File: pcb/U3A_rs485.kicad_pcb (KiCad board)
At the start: 2 copper layers, 34.5 x 26.4 mm, 17 parts, among them J1 Screw_Terminal_01x06, J2 Conn_01x07_Socket, J3 Conn_01x02_Pin, J4 Conn_01x08_Socket, J5 Conn_01x02_Pin, U1 THVD1452DR

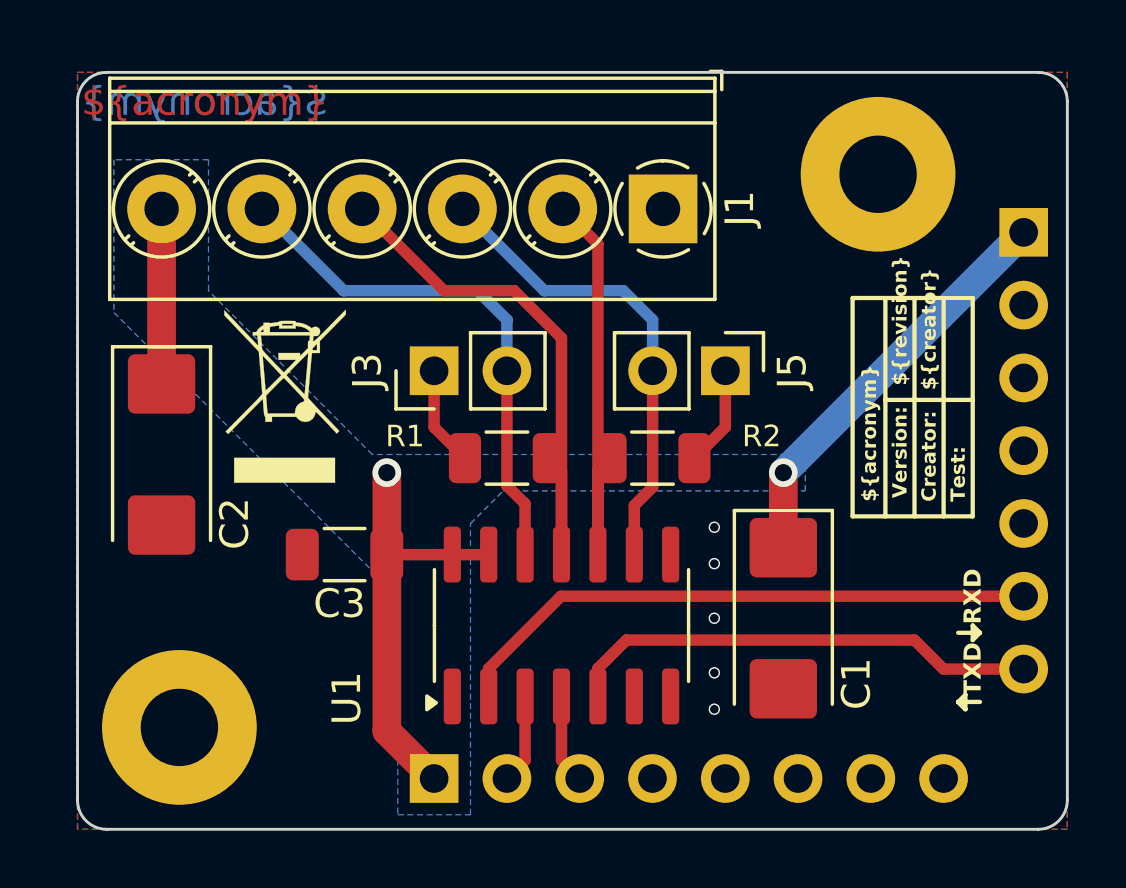
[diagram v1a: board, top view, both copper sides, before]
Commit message: Add missing pull-up resistor
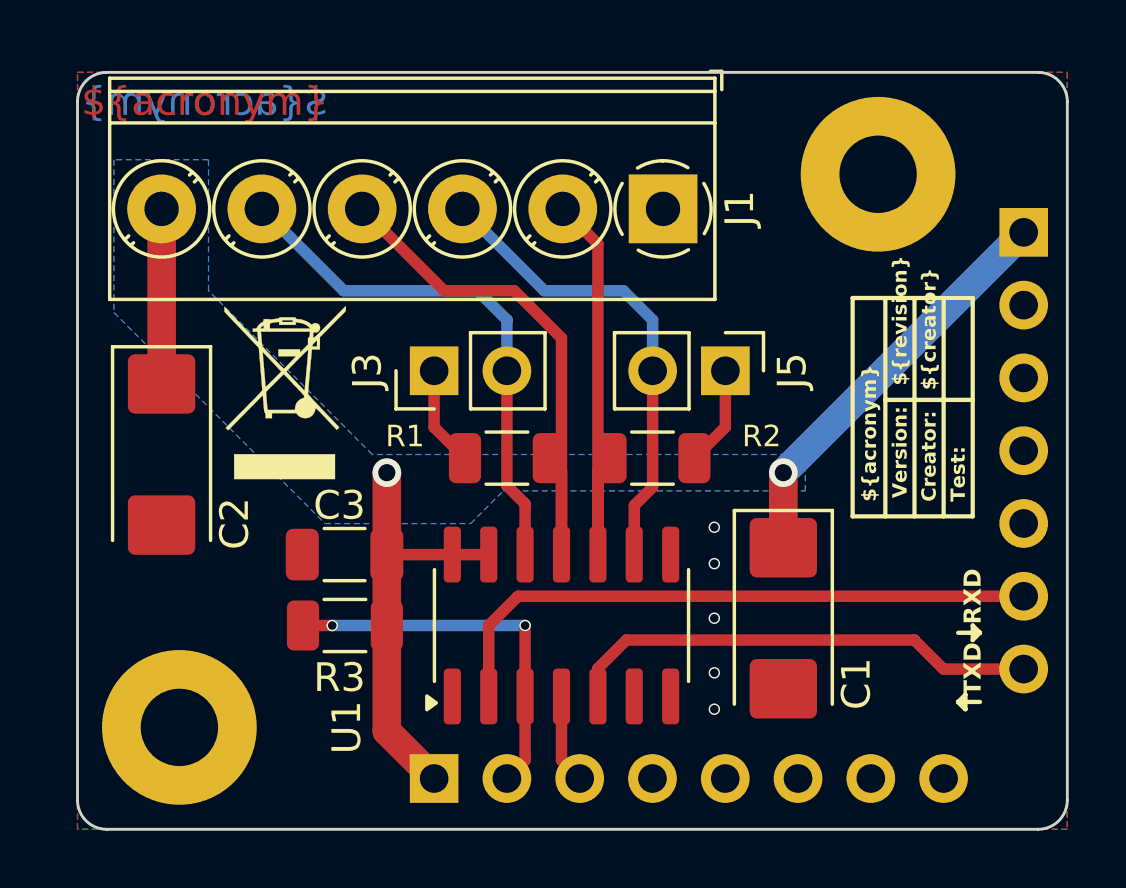
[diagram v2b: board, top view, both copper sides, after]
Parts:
- added R3: 10k, Resistor_SMD:R_1206_3216Metric, F.Cu at (154.1, 95.5)
- moved FID3 0.13 mm to (152.0, 87.4)
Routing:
- net /CBUS3: track 3.13 -> 13.4 mm, vias 0 -> 2
- net /RXD: track 20.7 -> 21.6 mm
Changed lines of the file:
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@@
   (net 20 "unconnected-(U1-NC-Pad1)")
   (net 21 "unconnected-(U1-NC-Pad8)")
+  (footprint "Resistor_SMD:R_1206_3216Metric" (layer "F.Cu")
+    (at 154.1125 95.504 180)
+    (descr "Resistor SMD 1206 (3216 Metric), square (rectangular) end terminal, IPC_7351 nominal, (Body size source: IPC-SM-782 page 72, https://www.pcb-3d.com/wordpress/wp-content/uploads/ipc-sm-782a_amendment_1_and_2.pdf), generated with kicad-footprint-generator")
+    (tags "resistor")
+    (property "Sheetfile" "U3A_rs485.kicad_sch")
+    (property "Sheetname" "")
+    (property "Vendor" "HTL")
+    (property "VendorId" "102967")
+    (property "ki_description" "Resistor")
+    (property "ki_keywords" "R res resistor")
+    (attr smd)
+    (fp_text reference "R3" (at 0.1885 -1.82) (layer "F.SilkS")
+        (effects (font (size 1 1) (thickness 0.15)))
+    )
+    (fp_text value "10k" (at 0 -1.778) (layer "F.Fab")
+        (effects (font (size 1 1) (thickness 0.15)))
+    )
+    (fp_text user "${REFERENCE}" (at 0 0) (layer "F.Fab")
+        (effects (font (size 0.8 0.8) (thickness 0.12)))
+    )
+    (fp_line (start -0.727064 -0.91) (end 0.727064 -0.91)
+      (stroke (width 0.12) (type solid)) (layer "F.SilkS"))
+    (fp_line (start -0.727064 0.91) (end 0.727064 0.91)
+      (stroke (width 0.12) (type solid)) (layer "F.SilkS"))
+    (fp_line (start -2.28 -1.12) (end 2.28 -1.12)
+      (stroke (width 0.05) (type solid)) (layer "F.CrtYd"))
+    (fp_line (start -2.28 1.12) (end -2.28 -1.12)
+      (stroke (width 0.05) (type solid)) (layer "F.CrtYd"))
+    (fp_line (start 2.28 -1.12) (end 2.28 1.12)
+      (stroke (width 0.05) (type solid)) (layer "F.CrtYd"))
+    (fp_line (start 2.28 1.12) (end -2.28 1.12)
+      (stroke (width 0.05) (type solid)) (layer "F.CrtYd"))
+    (fp_line (start -1.6 -0.8) (end 1.6 -0.8)
+      (stroke (width 0.1) (type solid)) (layer "F.Fab"))
+    (fp_line (start -1.6 0.8) (end -1.6 -0.8)
+      (stroke (width 0.1) (type solid)) (layer "F.Fab"))
+    (fp_line (start 1.6 -0.8) (end 1.6 0.8)
+      (stroke (width 0.1) (type solid)) (layer "F.Fab"))
+    (fp_line (start 1.6 0.8) (end -1.6 0.8)
+      (stroke (width 0.1) (type solid)) (layer "F.Fab"))
+    (pad "1" smd roundrect (at -1.4625 0 180) (size 1.125 1.75) (layers "F.Cu" "F.Paste" "F.Mask") (roundrect_rratio 0.222222)
+      (net 2 "VCC") (pintype "passive"))
+    (pad "2" smd roundrect (at 1.4625 0 180) (size 1.125 1.75) (layers "F.Cu" "F.Paste" "F.Mask") (roundrect_rratio 0.222222)
+      (net 8 "/CBUS3") (pintype "passive"))
+    (model "${KICAD6_3DMODEL_DIR}/Resistor_SMD.3dshapes/R_1206_3216Metric.wrl"
+      (offset (xyz 0 0 0))
+      (scale (xyz 1 1 1))
+      (rotate (xyz 0 0 0))
+    )
+  )
   (footprint "MountingHole:MountingHole_2.7mm_M2.5_Pad" (layer "F.Cu")
     (at 148.336 99.06)
@@
   )
   (footprint "Symbol:WEEE-Logo_4.2x6mm_SilkScreen" (layer "F.Cu")
-    (at 152.019 87.503)
+    (at 152.019 87.376)
     (descr "Waste Electrical and Electronic Equipment Directive")
     (tags "Logo WEEE")
@@
     (property "ki_keywords" "cap capacitor")
     (attr smd)
-    (fp_text reference "C3" (at -0.176 1.713) (layer "F.SilkS")
+    (fp_text reference "C3" (at -0.176 -1.716) (layer "F.SilkS")
         (effects (font (size 1 1) (thickness 0.15)))
     )
-    (fp_text value "100n" (at 0 1.85) (layer "F.Fab")
+    (fp_text value "100n" (at 0 -1.589) (layer "F.Fab")
         (effects (font (size 1 1) (thickness 0.15)))
     )
@@
     (property "ki_keywords" "THVD1452DR")
     (attr smd)
-    (fp_text reference "U1" (at -2.54 -7.493 90) (layer "F.SilkS")
+    (fp_text reference "U1" (at -3.556 -7.493 90) (layer "F.SilkS")
         (effects (font (size 1 1) (thickness 0.15)))
     )
@@
   (segment (start 161.671 100.208618) (end 162.306 100.843618) (width 0.4) (layer "F.Cu") (net 7))
   (segment (start 161.671 97.979) (end 161.671 100.208618) (width 0.4) (layer "F.Cu") (net 7))
+  (segment (start 160.401 97.979) (end 160.401 95.504) (width 0.4) (layer "F.Cu") (net 8))
   (segment (start 160.401 97.979) (end 160.401 100.208618) (width 0.4) (layer "F.Cu") (net 8))
+  (segment (start 152.65 95.504) (end 153.67 95.504) (width 0.4) (layer "F.Cu") (net 8))
   (segment (start 160.401 100.208618) (end 159.766 100.843618) (width 0.4) (layer "F.Cu") (net 8))
+  (via (at 153.67 95.504) (size 0.4) (drill 0.3) (layers "F.Cu" "B.Cu") (net 8))
+  (via (at 160.401 95.504) (size 0.4) (drill 0.3) (layers "F.Cu" "B.Cu") (net 8))
+  (segment (start 160.401 95.504) (end 153.67 95.504) (width 0.4) (layer "B.Cu") (net 8))
   (segment (start 177.795 86.868) (end 177.8 86.863) (width 0.4) (layer "B.Cu") (net 9))
-  (segment (start 177.8 94.483) (end 161.652001 94.483) (width 0.4) (layer "F.Cu") (net 10))
-  (segment (start 161.652001 94.483) (end 159.131 97.004001) (width 0.4) (layer "F.Cu") (net 10))
-  (segment (start 159.131 97.004001) (end 159.131 97.979) (width 0.4) (layer "F.Cu") (net 10))
+  (segment (start 159.131 95.504) (end 159.131 97.979) (width 0.4) (layer "F.Cu") (net 10))
+  (segment (start 160.152 94.483) (end 159.131 95.504) (width 0.4) (layer "F.Cu") (net 10))
+  (segment (start 177.8 94.483) (end 160.152 94.483) (width 0.4) (layer "F.Cu") (net 10))
   (segment (start 177.795 94.488) (end 177.8 94.483) (width 0.4) (layer "B.Cu") (net 10))
   (segment (start 173.99 96.012) (end 163.933001 96.012) (width 0.4) (layer "F.Cu") (net 11))
@@
     (polygon
       (pts
-        (xy 158.496 102.108)
+        (xy 158.496 91.948)
         (xy 158.496 91.948)
         (xy 159.639 90.805)
@@
         (xy 146.05 79.248)
         (xy 146.05 84.582)
-        (xy 155.956 94.488)
-        (xy 155.956 102.108)
+        (xy 153.416 91.948)
       )
     )
